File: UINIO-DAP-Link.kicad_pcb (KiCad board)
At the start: 2 copper layers, 90.4 x 31 mm, 49 parts, among them J1 扩展板串口 & 电源输出, J2 扩展板 JTAG 输出, J3 JTAG_nTRST 跳线选择, J4 3.3V 跳线选择, J5 扩展板 SWD 输入, J6 DAPLink 固件下载接口, J7 JTAG/SWD 下载接口, U1 ME6211, U2 STM32F103C8T6, Y1 Crystal_GND24

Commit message: Update PCB.
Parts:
- added R16: 5.1K, Resistor_SMD:R_0603_1608Metric, F.Cu at (113.5, 104.4)
- added R17: 5.1K, Resistor_SMD:R_0603_1608Metric, F.Cu at (113.5, 110.2)
- moved ? 0.34 mm to (128.0, 101.8)
- moved ? 0.30 mm to (130.2, 103.3)
- moved J6 0.15 mm to (106.8, 115.9)
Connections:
- USB1 pad A5: unconnected-(USB1-PadA5) -> Net-(R16-Pad2)
- USB1 pad B5: unconnected-(USB1-PadB5) -> Net-(R17-Pad2)
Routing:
- net GND: track 167.1 -> 186.3 mm
- net Net-(R16-Pad2): track 0.00 -> 3.72 mm
- net Net-(R17-Pad2): track 0.00 -> 3.40 mm
- net /Download_SWDIO: track 13.9 -> 15.0 mm
- net Net-(C4-Pad2): track 1.53 -> 2.52 mm
- net /Download_SWCLK: track 9.87 -> 10.7 mm
- net Net-(C3-Pad2): track 3.79 -> 4.35 mm
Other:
- board text added: "Version 3.2.0"
- board text removed: "Version 3.0.1"

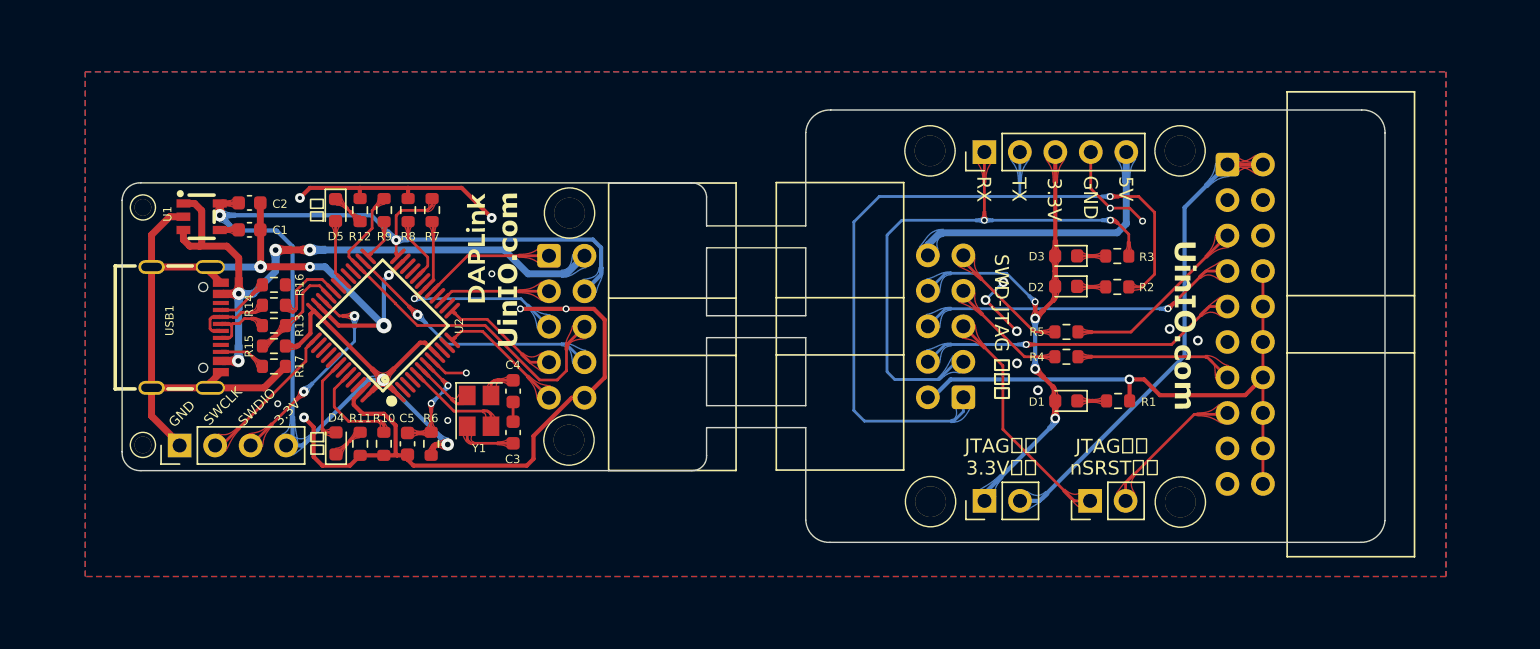
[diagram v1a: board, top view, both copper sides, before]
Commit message: Release UINIO-DAP-Link version 3.2.0.
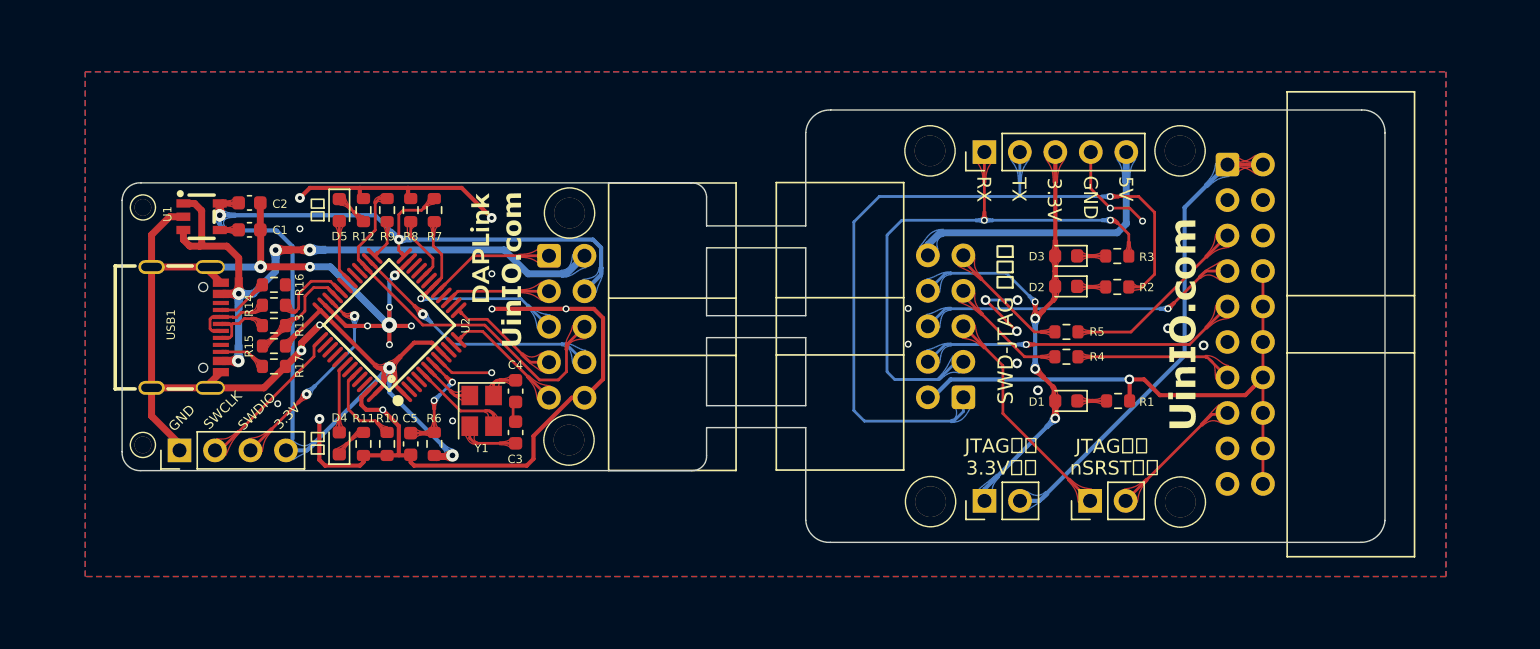
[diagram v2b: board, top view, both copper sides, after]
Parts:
- moved U2 0.46 mm to (121.8, 107.3)
- moved J6 0.35 mm to (106.8, 116.2)
- moved ? 0.30 mm to (128.3, 101.8)
- moved ? 0.28 mm to (130.5, 103.3)
- moved ? 0.27 mm to (178.6, 107.2), turned to 90 degrees
- moved D5 0.27 mm to (118.2, 99.0)
- moved R12 0.24 mm to (120.0, 99.0)
- moved D4 0.24 mm to (118.2, 115.8)
- moved R11 0.24 mm to (120.0, 115.8)
- moved R10 0.23 mm to (121.7, 115.8)
- moved C5 0.23 mm to (123.3, 115.8)
- moved R6 0.23 mm to (125.0, 115.8)
- moved R9 0.22 mm to (121.7, 99.0)
- moved R8 0.19 mm to (123.3, 99.0)
- moved C3 0.18 mm to (130.8, 115.0)
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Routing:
- net GND: track 186.3 -> 198.0 mm, vias 23 -> 33
- net /VDD_3.3V: track 97.5 -> 99.7 mm
- net Net-(D4-Pad2): track 6.14 -> 4.43 mm
- net Net-(R10-Pad1): track 7.32 -> 6.13 mm
- net Net-(U2-Pad6): track 4.46 -> 3.65 mm
- net /_JTAG_nSRST_Output: track 10.6 -> 9.86 mm
- net /Download_SWCLK: track 10.7 -> 9.99 mm
- net /_JTAG_nSRST_Input: track 16.9 -> 16.2 mm

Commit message: Prepare version 3.3.0.
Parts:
- removed the ? at (130.5, 103.3)
- removed the ? at (178.6, 107.2)
- removed the ? at (120.8, 107.3)
- removed the ? at (171.6, 107.2)
- added ?: LOGO, LOGO, B.Cu at (113.5, 107.4)
- added ?: LOGO, LOGO, B.Cu at (124.5, 107.4)
- added ?: LOGO, LOGO, B.Cu at (172.3, 107.4)
- moved USB1 0.20 mm to (107.1, 107.4)
- moved J2 0.18 mm to (181.8, 96.0)
- moved J6 0.16 mm to (107.0, 116.2)
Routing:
- net GND: track 198.0 -> 199.2 mm
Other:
- outline, holes or cut-outs redrawn
- board text added: "UinIO.com"
- board text added: "Version 3.3.0"
- board text removed: "Version 3.2.0"

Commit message: Prepare version 3.3.0.
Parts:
- moved HOLE1 0.29 mm to (104.2, 99.2)
- moved HOLE2 0.21 mm to (104.2, 115.7)
- moved HOLE3 0.14 mm to (134.7, 115.7)
- moved HOLE4 0.11 mm to (134.7, 99.2)
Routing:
- net GND: track 199.2 -> 201.2 mm
- net /3.3V_Output: track 33.6 -> 32.8 mm
